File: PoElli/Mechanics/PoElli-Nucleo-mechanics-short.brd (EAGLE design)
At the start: 57.5 x 70 mm, 30 parts, among them J1 DF12-ELLI-HEADER-TOP, J3 M022.54MM, J4 M022.54MM, T1 Coilcraft 230NL, T2 FLYBACK750311689, U1 ENC424J600, X1 M-BOLT-2, X2 M-BOLT-2, X3 M-BOLT-2, X4 M-BOLT-2

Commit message: Changes to PoElli-Nucleo-short from today's meeting
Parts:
- T2: value FLYBACK750311689 -> FLYBACKEMBEDDED; device ELL-i-Transformers:WE_EP13_SMD_10PIN -> ELL-i-Transformers:WE_EP13_SMD_10PIN_EMBEDDED
- moved U1 4.00 mm to (25.0, 36.0)
- moved U$2 1.41 mm to (59.0, 36.0)
- moved X1 1.00 mm to (9.50, 21.5)
- moved X2 1.00 mm to (9.50, 48.5)
- moved X3 1.00 mm to (52.5, 48.5)
- moved X4 1.00 mm to (52.5, 21.5)
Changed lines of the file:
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@@
 <layer number="220" name="220bmp" color="7" fill="1" visible="no" active="yes"/>
 <layer number="221" name="connection" color="7" fill="1" visible="no" active="yes"/>
+<layer number="222" name="222bmp" color="7" fill="1" visible="yes" active="yes"/>
 <layer number="223" name="223bmp" color="7" fill="1" visible="no" active="yes"/>
 <layer number="224" name="224bmp" color="7" fill="1" visible="no" active="yes"/>
@@
 <element name="D8" library="ELL-i-DIscreteSemi" package="DIODE-B2100" value="B2100" x="25" y="56"/>
 <element name="D7" library="ELL-i-DIscreteSemi" package="DIODE-B2100" value="B2100" x="25" y="48"/>
-<element name="T2" library="ELL-i-Transformers" package="WE_EP13_SMD_10PIN" value="FLYBACK750311689" x="39.57" y="54.15" rot="R180"/>
+<element name="T2" library="ELL-i-Transformers" package="WE_EP13_SMD_10PIN_EMBEDDED" value="FLYBACKEMBEDDED" x="39.57" y="54.15" rot="R180"/>
 <element name="J4" library="SparkFun-Connectors" package="1X02_2.54_SCREWTERM" value="M022.54MM" x="55.75" y="12.04" rot="R270"/>
 <element name="TP2" library="ELL-i-Passives" package="TP_5000" value="" x="3" y="65"/>
@@
 <element name="J3" library="SparkFun-Connectors" package="1X02_2.54_SCREWTERM" value="M022.54MM" x="54.76" y="60.08" rot="R270"/>
 <element name="D19" library="ELL-i-DIscreteSemi" package="DIODE-B2100" value="B2100" x="23" y="25"/>
-<element name="X1" library="ELL-i-Connectors" package="M2-1" value="M-BOLT-2" x="9.5" y="22.5"/>
-<element name="X2" library="ELL-i-Connectors" package="M2-1" value="M-BOLT-2" x="9.5" y="47.5"/>
-<element name="X3" library="ELL-i-Connectors" package="M2-1" value="M-BOLT-2" x="52.5" y="47.5"/>
-<element name="X4" library="ELL-i-Connectors" package="M2-1" value="M-BOLT-2" x="52.5" y="22.5"/>
+<element name="X1" library="ELL-i-Connectors" package="M2-1" value="M-BOLT-2" x="9.5" y="21.5"/>
+<element name="X2" library="ELL-i-Connectors" package="M2-1" value="M-BOLT-2" x="9.5" y="48.5"/>
+<element name="X3" library="ELL-i-Connectors" package="M2-1" value="M-BOLT-2" x="52.5" y="48.5"/>
+<element name="X4" library="ELL-i-Connectors" package="M2-1" value="M-BOLT-2" x="52.5" y="21.5"/>
 <element name="U$1" library="ELL-i-Boards" package="NUCLEO-SHIELD-UNDERSIDE-SHORT" value="NUCLEO-SHIELD" x="58" y="0" rot="R90"/>
-<element name="U1" library="ELL-i-DigitalIC" package="TQFP44-0.8MM" value="ENC424J600" x="21" y="36"/>
-<element name="U$2" library="ELL-i-Connectors" package="TE1888250" value="POE-TP-SHIELDED-LEDSTE1888250" x="58" y="35" rot="R90"/>
+<element name="U1" library="ELL-i-DigitalIC" package="TQFP44-0.8MM" value="ENC424J600" x="25" y="36"/>
+<element name="U$2" library="ELL-i-Connectors" package="TE1888250" value="POE-TP-SHIELDED-LEDSTE1888250" x="59" y="36" rot="R90"/>
 </elements>
 <signals>
@@
 <contactref element="T1" pad="10"/>
 <contactref element="U$2" pad="2"/>
-<wire x1="36.73" y1="24.511" x2="39.56" y2="32.46" width="0" layer="19" extent="1-1"/>
+<wire x1="36.73" y1="24.511" x2="40.56" y2="33.46" width="0" layer="19" extent="1-1"/>
 </signal>
 <signal name="N$2">
 <contactref element="T1" pad="9"/>
 <contactref element="U$2" pad="1"/>
-<wire x1="34.19" y1="24.511" x2="37.02" y2="31.444" width="0" layer="19" extent="1-1"/>
+<wire x1="34.19" y1="24.511" x2="38.02" y2="32.444" width="0" layer="19" extent="1-1"/>
 </signal>
 <signal name="N$3">
 <contactref element="T1" pad="13"/>
 <contactref element="U$2" pad="3"/>
-<wire x1="44.35" y1="24.511" x2="37.02" y2="33.476" width="0" layer="19" extent="1-1"/>
+<wire x1="44.35" y1="24.511" x2="38.02" y2="34.476" width="0" layer="19" extent="1-1"/>
 </signal>
 <signal name="N$4">
 <contactref element="T1" pad="14"/>
 <contactref element="U$2" pad="6"/>
-<wire x1="46.89" y1="24.511" x2="39.56" y2="36.524" width="0" layer="19" extent="1-1"/>
+<wire x1="46.89" y1="24.511" x2="40.56" y2="37.524" width="0" layer="19" extent="1-1"/>
 </signal>
 <signal name="POE_B-">
@@
 <contactref element="U$2" pad="5"/>
 <wire x1="19.15" y1="60" x2="22.85" y2="60" width="0" layer="19" extent="1-1"/>
-<wire x1="37.02" y1="35.508" x2="22.85" y2="60" width="0" layer="19" extent="1-1"/>
-<wire x1="39.56" y1="34.492" x2="37.02" y2="35.508" width="0" layer="19" extent="1-1"/>
+<wire x1="38.02" y1="36.508" x2="22.85" y2="60" width="0" layer="19" extent="1-1"/>
+<wire x1="40.56" y1="35.492" x2="38.02" y2="36.508" width="0" layer="19" extent="1-1"/>
 </signal>
 <signal name="N$21">
@@
 <contactref element="U$2" pad="GND@2"/>
 <contactref element="U$2" pad="GND@4"/>
-<wire x1="34.81" y1="41" x2="40.41" y2="43.045" width="0" layer="19" extent="1-1"/>
-<wire x1="34.81" y1="29" x2="34.81" y2="41" width="0" layer="19" extent="1-1"/>
-<wire x1="40.41" y1="26.946" x2="34.81" y2="29" width="0" layer="19" extent="1-1"/>
+<wire x1="35.81" y1="42" x2="41.41" y2="44.045" width="0" layer="19" extent="1-1"/>
+<wire x1="35.81" y1="30" x2="35.81" y2="42" width="0" layer="19" extent="1-1"/>
+<wire x1="41.41" y1="27.946" x2="35.81" y2="30" width="0" layer="19" extent="1-1"/>
 </signal>
 <signal name="N$10">
 <contactref element="U$2" pad="7"/>
 <contactref element="U$2" pad="8"/>
-<wire x1="37.02" y1="37.54" x2="39.56" y2="38.556" width="0" layer="19" extent="1-1"/>
+<wire x1="38.02" y1="38.54" x2="40.56" y2="39.556" width="0" layer="19" extent="1-1"/>
 </signal>
 </signals>

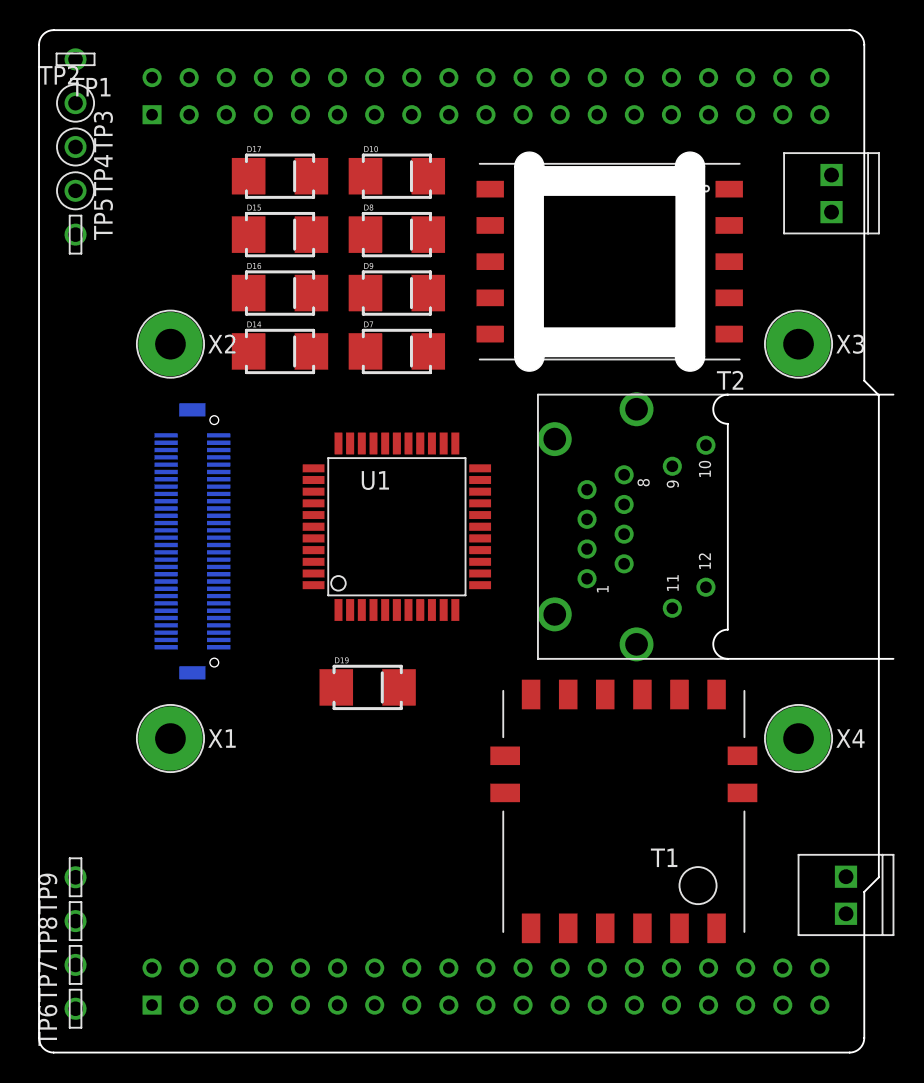
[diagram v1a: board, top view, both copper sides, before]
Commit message: Update Nucleo shield construction for Mechanics/PoElli-Nucleo-mechanics-short.{brd,sch}
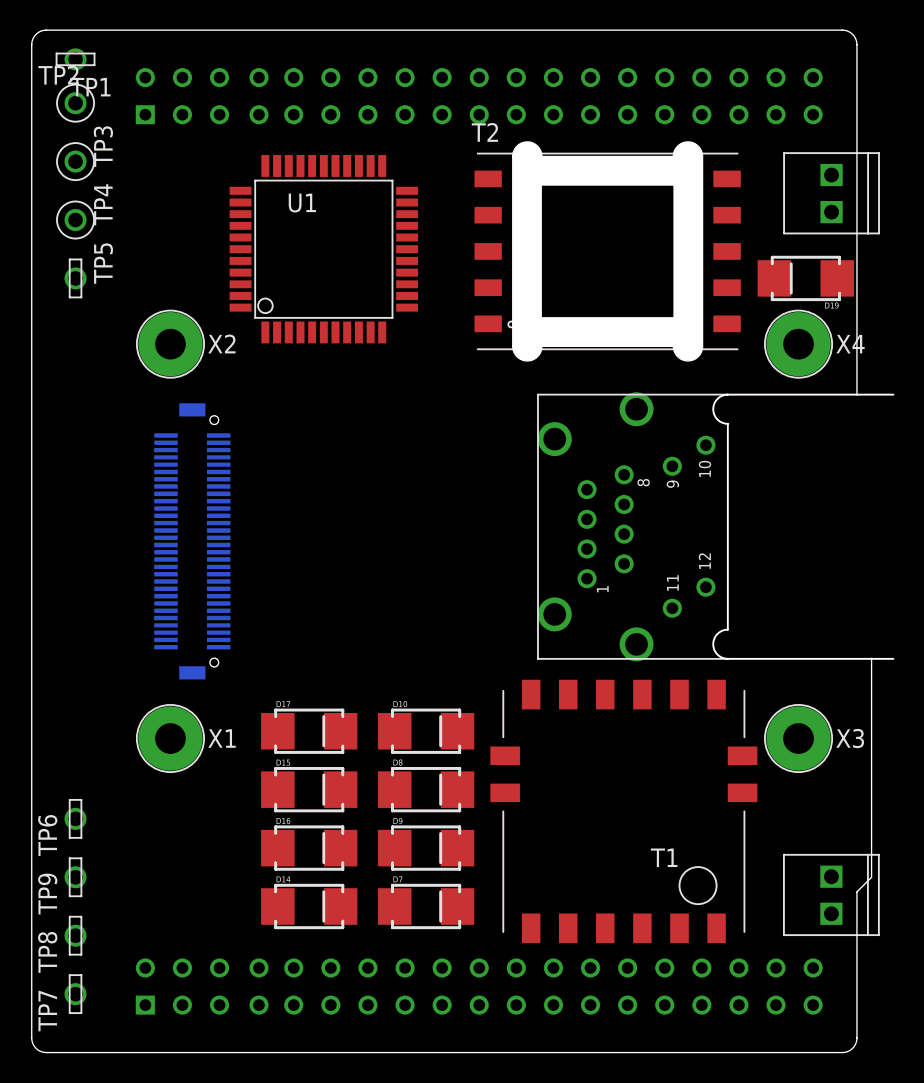
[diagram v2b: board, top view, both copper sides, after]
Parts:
- removed U$1: NUCLEO-SHIELD, ELL-i-Boards:NUCLEO-SHIELD-UNDERSIDE-SHORT
- added CN10: NUCLEO-CN10, ELL-i-Boards:NUCLEO-HEADER
- added CN7: NUCLEO-CN7, ELL-i-Boards:NUCLEO-HEADER
- added NUCLEO: NUCLEO-OUTLINE-SHORT, ELL-i-Boards:NUCLEO-SHIELD-UNDERSIDE-SHORT-OUTLINE
- moved D19 41.0 mm to (53.0, 53.0), turned to 180 degrees
- moved D10 38.1 mm to (27.0, 22.0)
- moved D14 38.1 mm to (19.0, 10.0)
- moved D15 38.1 mm to (19.0, 18.0)
- moved D16 38.1 mm to (19.0, 14.0)
- moved D17 38.1 mm to (19.0, 22.0)
- moved D7 38.1 mm to (27.0, 10.0)
- moved D8 38.1 mm to (27.0, 18.0)
- moved D9 38.1 mm to (27.0, 14.0)
- moved X3 27.0 mm to (52.5, 21.5)
- moved X4 27.0 mm to (52.5, 48.5)
- moved U1 19.6 mm to (20.0, 55.0)
- moved TP6 13.0 mm to (3.00, 16.0)
- moved TP5 3.00 mm to (3.00, 53.0)
- moved TP4 2.00 mm to (3.00, 57.0)
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- renumbered J1 to EXT1
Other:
- outline, holes or cut-outs redrawn

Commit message: Update Nucleo header origin to the center of the component
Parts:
- moved CN10 22.9 mm to (30.6, 65.5)
- moved CN7 22.9 mm to (30.6, 4.52)
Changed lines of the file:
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@@
 <layer number="111" name="111" color="7" fill="1" visible="no" active="yes"/>
 <layer number="112" name="tSilk" color="7" fill="1" visible="no" active="yes"/>
+<layer number="113" name="IDFDebug" color="4" fill="1" visible="yes" active="yes"/>
 <layer number="116" name="Patch_BOT" color="9" fill="4" visible="no" active="yes"/>
 <layer number="118" name="Rect_Pads" color="7" fill="1" visible="no" active="yes"/>
@@
 <element name="U1" library="ELL-i-DigitalIC" package="TQFP44-0.8MM" value="ENC424J600" x="20" y="55"/>
 <element name="U$2" library="ELL-i-Connectors" package="TE1888250" value="POE-TP-SHIELDED-LEDSTE1888250" x="59" y="36" rot="R90"/>
-<element name="CN7" library="ELL-i-Boards" package="NUCLEO-HEADER" value="NUCLEO-CN7" x="7.78" y="3.25"/>
-<element name="CN10" library="ELL-i-Boards" package="NUCLEO-HEADER" value="NUCLEO-CN10" x="7.78" y="64.21"/>
+<element name="CN7" library="ELL-i-Boards" package="NUCLEO-HEADER" value="NUCLEO-CN7" x="30.64" y="4.52"/>
+<element name="CN10" library="ELL-i-Boards" package="NUCLEO-HEADER" value="NUCLEO-CN10" x="30.64" y="65.48"/>
 <element name="NUCLEO" library="ELL-i-Boards" package="NUCLEO-SHIELD-UNDERSIDE-SHORT-OUTLINE" value="NUCLEO-OUTLINE-SHORT" x="0" y="0"/>
 </elements>
